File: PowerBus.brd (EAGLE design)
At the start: 100 x 80 mm, 23 parts, among them U1 TSR_1-24120, X1 5566-2, X10 5566-4, X11 5566-4, X12 5566-4, X2 5566-2, X3 5566-2, X4 5566-2, X5 5566-2, X6 5566-4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

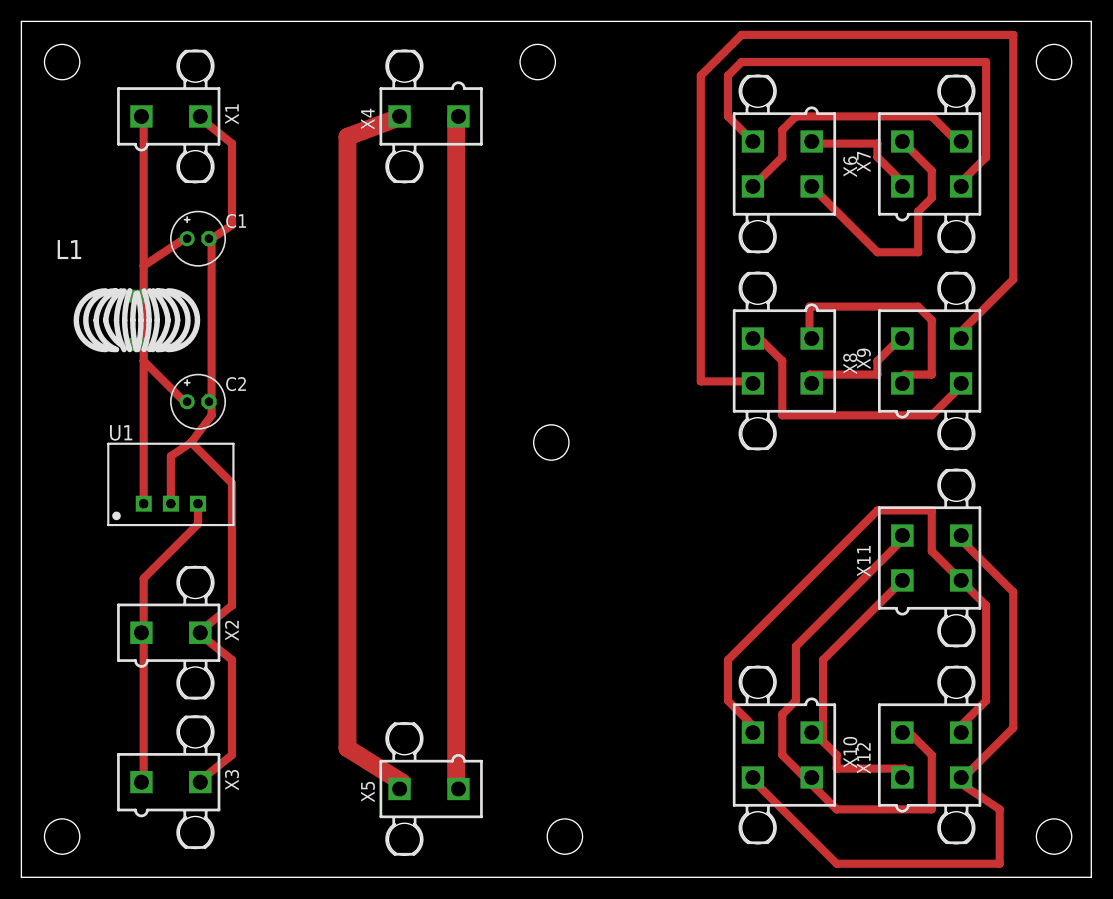
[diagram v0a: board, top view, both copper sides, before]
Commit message: PM - Updated schematic and board. Initial prototype from OSHPark
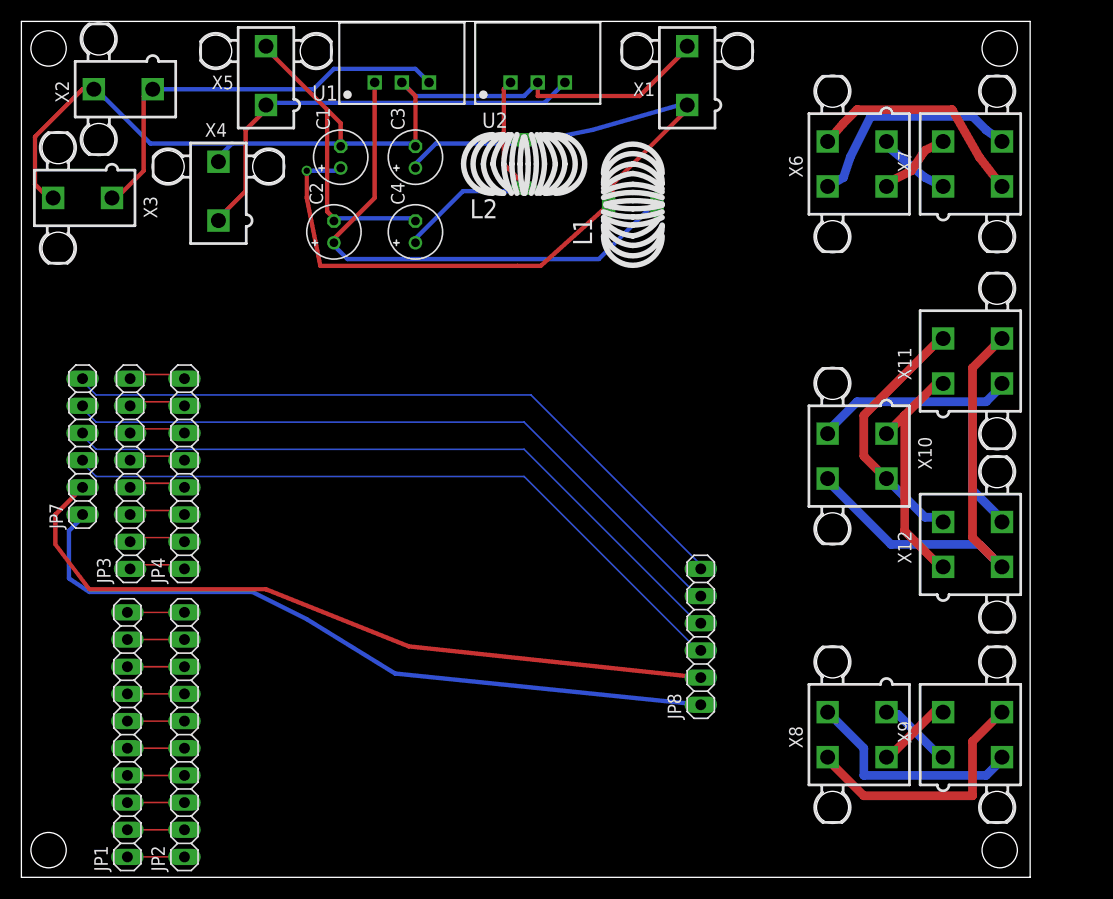
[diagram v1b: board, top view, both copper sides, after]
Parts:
- removed U$3, U$6, U$7: (no value), SparkFun-Electromechanical:STAND-OFF
- added C3, C4: 4.7uF/50V, rcl:E2-5
- added JP1, JP2: (no value), pinhead:1X10
- added JP3, JP4: (no value), pinhead:1X08
- added JP7, JP8: (no value), pinhead:1X06
- added L2: 8.2uH/.02ohm/2A, inductor-multicomp:MCAP103722016A-8R2MU
- added U2: TSR_1-2490, _traco_tsr-1:TSR-1
- moved X5 68.4 mm to (22.9, 74.9), turned to 0 degrees
- moved X3 55.2 mm to (5.71, 63.5), turned to 90 degrees
- moved X2 51.0 mm to (9.53, 73.7), turned to 90 degrees
- moved X1 48.4 mm to (62.2, 74.9), turned to 0 degrees
- moved L1 47.6 mm to (57.1, 62.9), turned to 90 degrees
- moved U1 44.9 mm to (35.6, 74.3)
- moved X8 35.6 mm to (78.1, 13.3)
- moved X9 35.1 mm to (88.9, 13.3)
- moved X10 28.8 mm to (78.1, 39.4)
- moved X4 20.9 mm to (18.4, 64.1), turned to 0 degrees
- moved C2 20.3 mm to (29.2, 60.3), turned to 90 degrees
- moved X12 20.1 mm to (88.9, 31.1)
- moved X11 18.8 mm to (88.9, 48.3)
- moved C1 15.4 mm to (29.8, 67.3), turned to 90 degrees
- moved X6 6.98 mm to (78.1, 66.7)
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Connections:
- new net N$15: JP1.3, JP2.3
- new net N$16: JP1.5, JP2.5
- new net N$17: JP1.6, JP2.6
- new net N$18: JP1.7, JP2.7
- new net N$19: JP1.8, JP2.8
- new net N$20: JP1.9, JP2.9
- new net N$21: JP1.10, JP2.10
- new net N$22: JP1.4, JP2.4
- new net N$24: JP3.1, JP4.1
- new net N$25: JP3.2, JP4.2
- new net N$26: JP3.3, JP4.3
- new net N$27: JP3.4, JP4.4
- new net N$28: JP3.5, JP4.5
- new net N$29: JP3.6, JP4.6
- new net N$30: JP3.7, JP4.7
- new net N$31: JP3.8, JP4.8
- new net N$39: JP7.1, JP8.1
- new net N$40: JP7.2, JP8.2
- new net N$41: JP7.3, JP8.3
- new net N$42: JP7.4, JP8.4
- new net N$43: JP7.5, JP8.5
- new net N$44: JP7.6, JP8.6
- new net VI2: C2.+, L1.2, U1.1
- new net VI3: C4.+, L2.2, U2.1
- new net VO2: U2.3, X4.1, X5.1
- net GND: now also C3.-, C4.-, U2.2, X4.2, X5.2
- net N$5: now also JP1.1, JP2.1; no longer X4.1, X5.1
- net N$6: now also JP1.2, JP2.2; no longer X4.2, X5.2
- net VI: now also C3.+, L2.1; no longer C2.+, L1.2, U1.1
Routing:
- net N$10: track 95.3 -> 24.1 mm
- net N$40: track 0.00 -> 70.0 mm
- net N$39: track 0.00 -> 68.1 mm
- net N$43: track 0.00 -> 65.5 mm
- net N$42: track 0.00 -> 65.5 mm
- net N$44: track 0.00 -> 65.5 mm
- net N$41: track 0.00 -> 65.5 mm
- net N$6: track 69.4 -> 5.33 mm
- net N$5: track 63.1 -> 5.33 mm
- net VI2: track 0.00 -> 49.6 mm
- net VO2: track 0.00 -> 41.6 mm
- net GND: track 79.4 -> 117.7 mm
- net VI: track 48.3 -> 81.6 mm, vias 0 -> 1
- net N$12: track 51.1 -> 24.1 mm
- net N$13: track 57.0 -> 30.8 mm
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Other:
- board size 100 x 80 mm -> 94.3 x 80 mm
